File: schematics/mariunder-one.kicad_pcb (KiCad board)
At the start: 2 copper layers, 190.5 x 73.7 mm, 44 parts, among them J1 Conn_01x07_I2S, J2 USB_A, J3 Conn_01x02, J4 Conn_02x04_C1101, Q1 2N3904, SW1 SW_Push_Dual_UP, SW10 SW_Push_Dual_BTN_A, SW11 SW_SPDT, SW2 SW_Push_Dual_DOWN, SW3 SW_Push_Dual_LEFT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

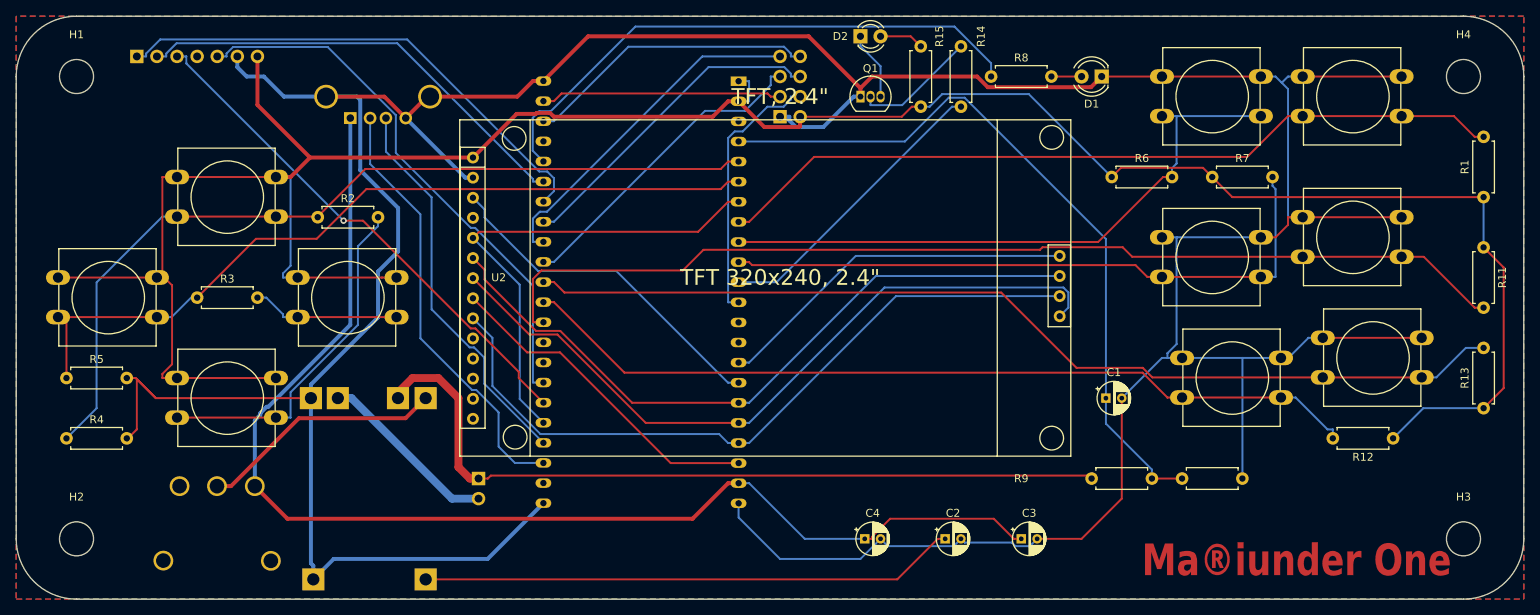
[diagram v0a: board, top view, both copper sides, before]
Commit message: Switched btn a,b, select and start to ADC2 as GPIO 35,36 and 37 are used in octal PSRAM mode
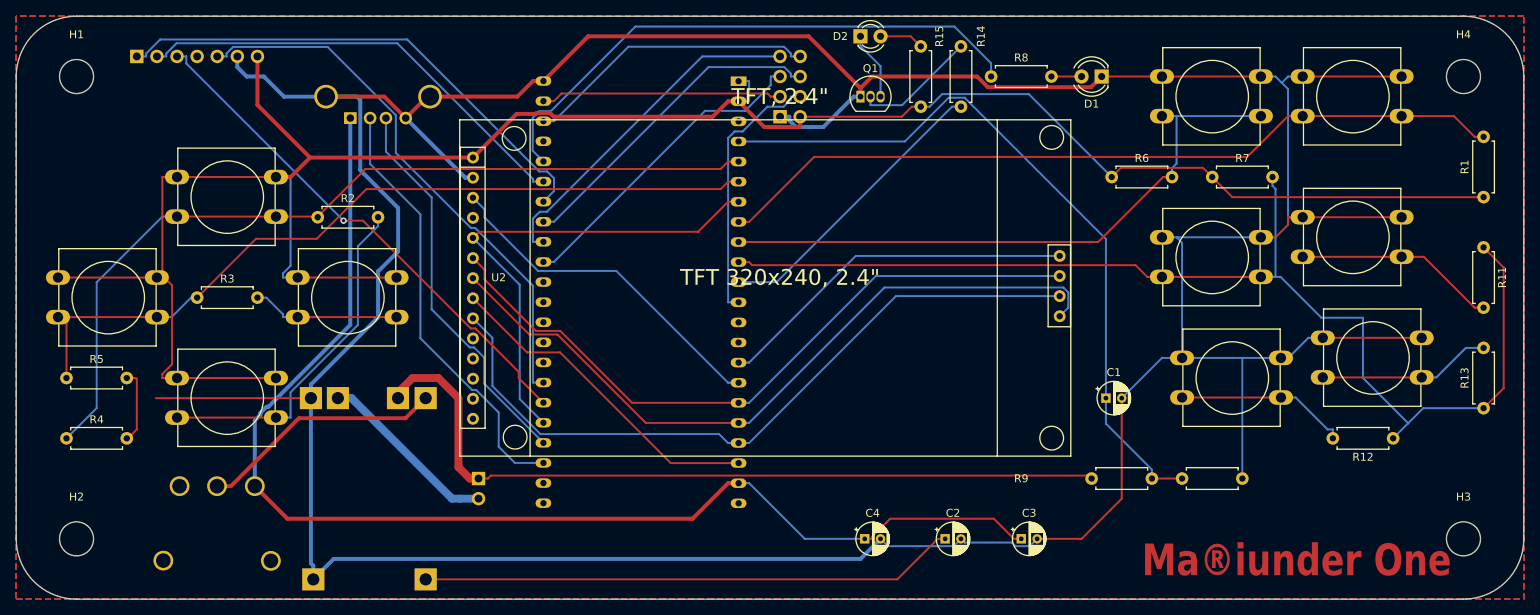
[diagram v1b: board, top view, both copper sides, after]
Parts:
- R11: value 10K -> 5K
- R13: value 10K -> 50K
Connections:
- R11 pad 1: /+3.3V -> /PAD_ADC
- R11 pad 2: /START -> Net-(SW8A-D)
- R12 pad 1: /+3.3V -> /PAD_ADC
- R12 pad 2: /BTN_B -> Net-(SW9A-D)
- R13 pad 1: /+3.3V -> /PAD_ADC
- R13 pad 2: /BTN_A -> Net-(SW10A-D)
- R7 pad 2: /SEL -> /PAD_ADC
- SW10 pad 2: /BTN_A -> Net-(SW10A-D)
- SW7 pad 2: /SEL -> /PAD_ADC
- SW8 pad 2: /START -> Net-(SW8A-D)
- SW9 pad 2: /BTN_B -> Net-(SW9A-D)
- U1 pad 10: /SEL -> /PAD_ADC
- U1 pad 22: GND -> unconnected-(U1-GND-Pad22)
- U1 pad 23: GND -> unconnected-(U1-GND-Pad23)
- U1 pad 32: /START -> unconnected-(U1-GPIO35-Pad32)
- U1 pad 33: /BTN_B -> unconnected-(U1-GPIO36-Pad33)
- U1 pad 34: /BTN_A -> unconnected-(U1-GPIO37-Pad34)
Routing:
- net /PAD_ADC: track 0.00 -> 145.7 mm
- net /START: track 131.8 -> 0.00 mm
- net /BTN_A: track 125.3 -> 0.00 mm
- net /BTN_B: track 107.5 -> 0.00 mm
- net /SEL: track 81.4 -> 0.00 mm
- net /+3.3V: track 327.6 -> 285.8 mm
- net Net-(SW8A-D): track 0.00 -> 25.5 mm
- net Net-(SW10A-D): track 0.00 -> 21.9 mm
- net Net-(SW9A-D): track 0.00 -> 21.8 mm
- net GND: track 520.2 -> 531.0 mm
